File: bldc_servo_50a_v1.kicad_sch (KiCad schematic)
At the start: 130 parts, among them IC1 DRV8305NQPHPRQ1, IC2 TPS22919DCKR, J1 CAN1, J2 CAN2, J3 SWD, J4 SWD, J5 FAN, P1 PVDD, P2 GND, P3 PHASE_A, P4 PHASE_B, P5 PHASE_C, Q1 BSC010N04LS, Q2 BSC010N04LS, Q3 BSC010N04LS, Q4 BSC010N04LS, Q5 BSC010N04LS, Q6 BSC010N04LS, U1 TLV75533PDBV, U2 SN65HVD230, U3 LMR51430, U5 STM32G431CBT6

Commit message: Wip: before fixing footprints
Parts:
- added C54, C55, C56: 1n, Capacitor_SMD:C_0402_1005Metric_Pad0.74x0.62mm_HandSolder, symbol Device:C_Small
- L1: value 3.3uH -> 3.3u
- renumbered C45 to C1, C13 to C10, C14 to C11, C15 to C12, C27 to C13, C50 to C14, C17 to C15, C38 to C16, C40 to C17, C41 to C18, C51 to C19, C44 to C2, C52 to C20, C19 to C21, C20 to C22, C21 to C23, C22 to C24, C23 to C25, C30 to C26, C32 to C27, C29 to C28, C39 to C29, C46 to C3, C8 to C30, C5 to C31, C1 to C32, C7 to C33, C9 to C34, C3 to C35, C2 to C36, C6 to C37, C28 to C38, C34 to C39, C47 to C4, C36 to C40, C33 to C41, C35 to C42, C31 to C43, C12 to C44, C16 to C45, C18 to C46, C43 to C47, C42 to C48, C37 to C49, C48 to C5, C24 to C50, C25 to C51, C26 to C52, C49 to C6, C10 to C7, C4 to C8, C11 to C9, D2 to D1, D3 to D2, D6 to D3, D7 to D6, J5 to J3, J3 to J4, J4 to J5, NT5 to NT1, NT11 to NT10, NT3 to NT11, NT4 to NT2, NT6 to NT3, NT1 to NT4, NT7 to NT5, NT8 to NT6, NT2 to NT7, NT9 to NT8, NT10 to NT9, R5 to R1, R6 to R10, R28 to R11, R3 to R12, R4 to R13, R19 to R14, R20 to R15, R14 to R16, R29 to R17, R31 to R18, R33 to R19, R9 to R2, R35 to R20, R30 to R21, R32 to R22, R34 to R23, R36 to R24, R15 to R25, R16 to R26, R17 to R27, R23 to R28, R18 to R3, R1 to R4, R2 to R5, R7 to R6, R8 to R7, R12 to R8, R13 to R9, U5 to U1, IC1 to U2, U1 to U4, U2 to U5, IC2 to U6
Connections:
- net PWRGD is gone; now on net DRV_PWRGD: U1.25 (PB11)
- net WAKE is gone; now on net DRV_WAKE: U1.3 (PC14)
- net +3.3V: now also C21.2, C22.2, C23.2, C24.2, C25.2; no longer C21.1, C22.1, C23.1, C24.1, C25.1
- net +5V: now also L1.1; no longer L1.2
- net 5V_SW: now also L1.2; no longer L1.1
- net DRV_WAKE: no longer U1.40 (PB3)
- net FAN_EN: now also U1.44 (PB7)
- net GND: now also C21.1, C22.1, C23.1, C24.1, C25.1, C54.2, C55.2, C56.2; no longer C21.2, C22.2, C23.2, C24.2, C25.2
- net PHASE_A_SENSE: now also U1.10 (PA2); no longer U1.11 (PA3)
- net PHASE_B_SENSE: now also U1.11 (PA3); no longer U1.5 (PF0)
- net PVDD_SENSE: now also U1.5 (PF0); no longer U1.6 (PF1)
- net SO1: now also U1.6 (PF1); no longer U1.8 (PA0)
- net SO2: now also U1.8 (PA0); no longer U1.9 (PA1)
- net SO3: now also U1.9 (PA1); no longer U1.10 (PA2)
- net at NT1.2, NT2.2, Q2.1 (S_1)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: now also C54.1
- net BOOT0: now reaches U1.45 (PB8)
- net at NT5.2, NT6.2, Q4.1 (S_1)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: now also C55.1
- net at NT10.2, NT9.2, Q6.1 (S_1)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: now also C56.1
- net FAN renamed FAN_PWM
- net SCLK renamed SCK
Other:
- note added: "3.3V LDO"
- note added: "5V BUCK CONVERTER"
- note added: "CAN TRANSCEIVER"
- note added: "DRIVER"
- note added: "FAN CONTROL"
- note added: "LED"
- note added: "MAIN VOLTAGE CAPACITORS"
- note added: "MOSFETS"
- note added: "MOUNTING HOLES"
- note added: "TEMPERATURE SENSING"
- note added: "VOLTAGE SENSING"
- note added: "tentative"
- note removed: "5v regulator"
- note removed: "Addressable LED"
- note removed: "CAN Transceiver"
- note removed: "DRV8305"
- note removed: "Encoder Connectors"
- note removed: "LDO (5v->3v3)"
- note removed: "MCU Decoupling caps"
- note removed: "Mosfets"
- note removed: "Phase Voltage Sensing"
- note removed: "RC Snubber"
- note removed: "SWD"
- note removed: "Thermistor"
- moved on the sheet: C1, C10, C11, C12, C13, C14, C15, C16, C17, C18, C19, C2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

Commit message: Schematic done
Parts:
- FPC1, FPC2: footprint HCTL HC-FPC-05-09-8RLTAG_8pin connector:FPC-SMD_8P-P0.50_HC-FPC-05-09-8RLTAG -> HCTL HC-FPC-05-09-8RLTAG:FPC-SMD_8P-P0.50_HC-FPC-05-09-8RLTAG
- U6: footprint SOT65P210X110-6N -> TPS22919DCKR:SOT65P210X110-6N
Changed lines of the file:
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@@
 			)
 		)
-		(property "Footprint" "HCTL HC-FPC-05-09-8RLTAG_8pin connector:FPC-SMD_8P-P0.50_HC-FPC-05-09-8RLTAG"
+		(property "Footprint" "HCTL HC-FPC-05-09-8RLTAG:FPC-SMD_8P-P0.50_HC-FPC-05-09-8RLTAG"
 			(at 322.58 154.94 0)
 			(effects
@@
 			)
 		)
-		(property "Footprint" "HCTL HC-FPC-05-09-8RLTAG_8pin connector:FPC-SMD_8P-P0.50_HC-FPC-05-09-8RLTAG"
+		(property "Footprint" "HCTL HC-FPC-05-09-8RLTAG:FPC-SMD_8P-P0.50_HC-FPC-05-09-8RLTAG"
 			(at 322.58 115.57 0)
 			(effects
@@
 			)
 		)
-		(property "Footprint" "SOT65P210X110-6N"
+		(property "Footprint" "TPS22919DCKR:SOT65P210X110-6N"
 			(at 232.41 220.65 0)
 			(effects

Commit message: Some small changes
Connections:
- net NFAULT is gone; now on net DRV_NFAULT: U1.22 (PB10), U2.8 (NFAULT)
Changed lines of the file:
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@@
 	(wire
 		(pts
-			(xy 24.13 63.5) (xy 31.75 63.5)
+			(xy 21.59 63.5) (xy 31.75 63.5)
 		)
 		(stroke
@@
 	(wire
 		(pts
-			(xy 24.13 83.82) (xy 31.75 83.82)
+			(xy 21.59 83.82) (xy 31.75 83.82)
 		)
 		(stroke
@@
 	(wire
 		(pts
-			(xy 24.13 71.12) (xy 31.75 71.12)
+			(xy 21.59 71.12) (xy 31.75 71.12)
 		)
 		(stroke
@@
 	(wire
 		(pts
-			(xy 24.13 73.66) (xy 31.75 73.66)
+			(xy 21.59 73.66) (xy 31.75 73.66)
 		)
 		(stroke
@@
 	(wire
 		(pts
-			(xy 24.13 68.58) (xy 31.75 68.58)
+			(xy 21.59 68.58) (xy 31.75 68.58)
 		)
 		(stroke
@@
 	(wire
 		(pts
-			(xy 24.13 81.28) (xy 31.75 81.28)
-		)
-		(stroke
-			(width 0)
-			(type default)
-		)
-	)
-	(wire
-		(pts
 			(xy 335.28 100.33) (xy 351.79 100.33)
 		)
@@
 	(wire
 		(pts
-			(xy 24.13 86.36) (xy 31.75 86.36)
+			(xy 21.59 86.36) (xy 31.75 86.36)
 		)
 		(stroke
@@
 	(wire
 		(pts
-			(xy 24.13 88.9) (xy 31.75 88.9)
+			(xy 21.59 88.9) (xy 31.75 88.9)
 		)
 		(stroke
@@
 	(wire
 		(pts
-			(xy 24.13 78.74) (xy 31.75 78.74)
+			(xy 21.59 78.74) (xy 31.75 78.74)
 		)
 		(stroke
@@
 	(wire
 		(pts
-			(xy 24.13 76.2) (xy 31.75 76.2)
+			(xy 21.59 76.2) (xy 31.75 76.2)
 		)
 		(stroke
@@
 	(wire
 		(pts
-			(xy 24.13 91.44) (xy 31.75 91.44)
+			(xy 21.59 91.44) (xy 31.75 91.44)
 		)
 		(stroke
@@
 	(wire
 		(pts
+			(xy 21.59 81.28) (xy 31.75 81.28)
+		)
+		(stroke
+			(width 0)
+			(type default)
+		)
+	)
+	(wire
+		(pts
 			(xy 226.06 201.93) (xy 234.95 201.93)
 		)
@@
 	(wire
 		(pts
-			(xy 24.13 66.04) (xy 31.75 66.04)
+			(xy 21.59 66.04) (xy 31.75 66.04)
 		)
 		(stroke
@@
 	)
 	(label "INHA"
-		(at 24.13 66.04 0)
+		(at 21.59 66.04 0)
 		(effects
 			(font
@@
 	)
 	(label "MOSI"
-		(at 24.13 86.36 0)
+		(at 21.59 86.36 0)
 		(effects
 			(font
@@
 	)
 	(label "DRV_CS"
-		(at 24.13 83.82 0)
+		(at 21.59 83.82 0)
 		(effects
 			(font
@@
 		)
 	)
+	(label "DRV_NFAULT"
+		(at 335.28 87.63 0)
+		(effects
+			(font
+				(size 1.27 1.27)
+			)
+			(justify left bottom)
+		)
+	)
 	(label "SL_C"
 		(at 83.82 88.9 180)
@@
 	)
 	(label "INLC"
-		(at 24.13 78.74 0)
+		(at 21.59 78.74 0)
 		(effects
 			(font
@@
 		)
 	)
-	(label "NFAULT"
-		(at 24.13 81.28 0)
-		(effects
-			(font
-				(size 1.27 1.27)
-			)
-			(justify left bottom)
-		)
-	)
 	(label "DRV_AVDD"
 		(at 16.51 152.4 0)
@@
 	)
 	(label "INHB"
-		(at 24.13 71.12 0)
+		(at 21.59 71.12 0)
 		(effects
 			(font
@@
 	)
 	(label "INLA"
-		(at 24.13 68.58 0)
+		(at 21.59 68.58 0)
 		(effects
 			(font
@@
 		)
 	)
+	(label "DRV_NFAULT"
+		(at 21.59 81.28 0)
+		(effects
+			(font
+				(size 1.27 1.27)
+			)
+			(justify left bottom)
+		)
+	)
 	(label "FAN_PWM"
 		(at 218.44 102.87 180)
@@
 	)
 	(label "SCK"
-		(at 24.13 91.44 0)
+		(at 21.59 91.44 0)
 		(effects
 			(font
@@
 	)
 	(label "INHC"
-		(at 24.13 76.2 0)
+		(at 21.59 76.2 0)
 		(effects
 			(font
@@
 	)
 	(label "MISO"
-		(at 24.13 88.9 0)
+		(at 21.59 88.9 0)
 		(effects
 			(font
@@
 	)
 	(label "EN_GATE"
-		(at 24.13 63.5 0)
+		(at 21.59 63.5 0)
 		(effects
 			(font
@@
 		)
 	)
-	(label "NFAULT"
-		(at 335.28 87.63 0)
-		(effects
-			(font
-				(size 1.27 1.27)
-			)
-			(justify left bottom)
-		)
-	)
 	(label "SH_C"
 		(at 138.4256 223.52 0)
@@
 	)
 	(label "INLB"
-		(at 24.13 73.66 0)
+		(at 21.59 73.66 0)
 		(effects
 			(font
@@
 	(symbol
 		(lib_id "power:PWR_FLAG")
-		(at 383.54 267.97 270)
+		(at 393.7 266.7 270)
 		(unit 1)
 		(exclude_from_sim no)
@@
 		(dnp no)
 		(property "Reference" "#FLG04"
-			(at 385.445 267.97 0)
+			(at 395.605 266.7 0)
 			(effects
 				(font
@@
 		)
 		(property "Value" "PWR_FLAG"
-			(at 387.096 267.97 0)
+			(at 397.256 266.7 0)
 			(effects
 				(font
@@
 		)
 		(property "Footprint" ""
-			(at 383.54 267.97 0)
+			(at 393.7 266.7 0)
 			(effects
 				(font
@@
 		)
 		(property "Datasheet" "~"
-			(at 383.54 267.97 0)
+			(at 393.7 266.7 0)
 			(effects
 				(font
@@
 		)
 		(property "Description" "Special symbol for telling ERC where power comes from"
-			(at 383.54 267.97 0)
+			(at 393.7 266.7 0)
 			(effects
 				(font
@@
 	(symbol
 		(lib_id "power:+3V3")
-		(at 383.54 267.97 0)
+		(at 393.7 266.7 0)
 		(unit 1)
 		(exclude_from_sim no)
@@
 		(dnp no)
 		(property "Reference" "#PWR055"
-			(at 383.54 271.78 0)
+			(at 393.7 270.51 0)
 			(effects
 				(font
@@
 		)
 		(property "Value" "+3V3"
-			(at 383.54 264.414 0)
+			(at 393.7 263.144 0)
 			(effects
 				(font
@@
 		)
 		(property "Footprint" ""
-			(at 383.54 267.97 0)
+			(at 393.7 266.7 0)
 			(effects
 				(font
@@
 		)
 		(property "Datasheet" ""
-			(at 383.54 267.97 0)
+			(at 393.7 266.7 0)
 			(effects
 				(font
@@
 		)
 		(property "Description" "Power symbol creates a global label with name \"+3V3\""
-			(at 383.54 267.97 0)
+			(at 393.7 266.7 0)
 			(effects
 				(font

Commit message: Tentative placement of FETs in PCB
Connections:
- net SN1: now also NT4.1; no longer NT2.1
- net SN2: now also NT7.1; no longer NT6.1
- net SN3: now also NT11.1; no longer NT10.1
- net SP1: now also NT2.1; no longer NT4.1
- net SP2: now also NT6.1; no longer NT7.1
- net SP3: now also NT10.1; no longer NT11.1

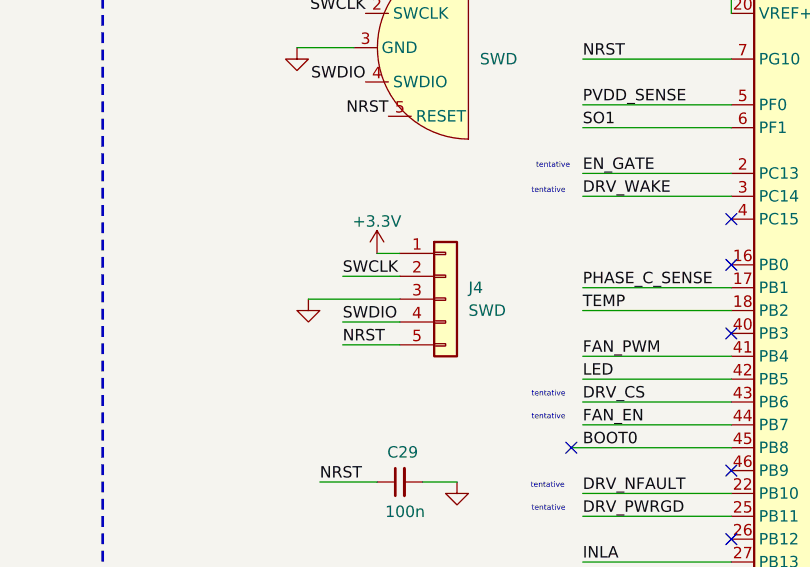
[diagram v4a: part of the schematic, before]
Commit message: Placing DRV, Bulk caps, FETs
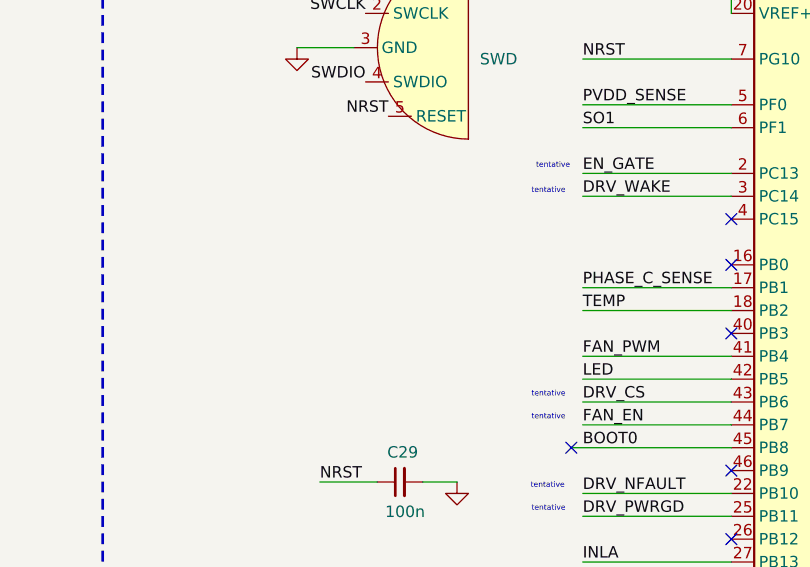
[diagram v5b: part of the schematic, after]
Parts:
- removed J4: SWD, Connector_PinHeader_2.54mm:PinHeader_1x05_P2.54mm_Vertical, symbol Connector_Generic:Conn_01x05

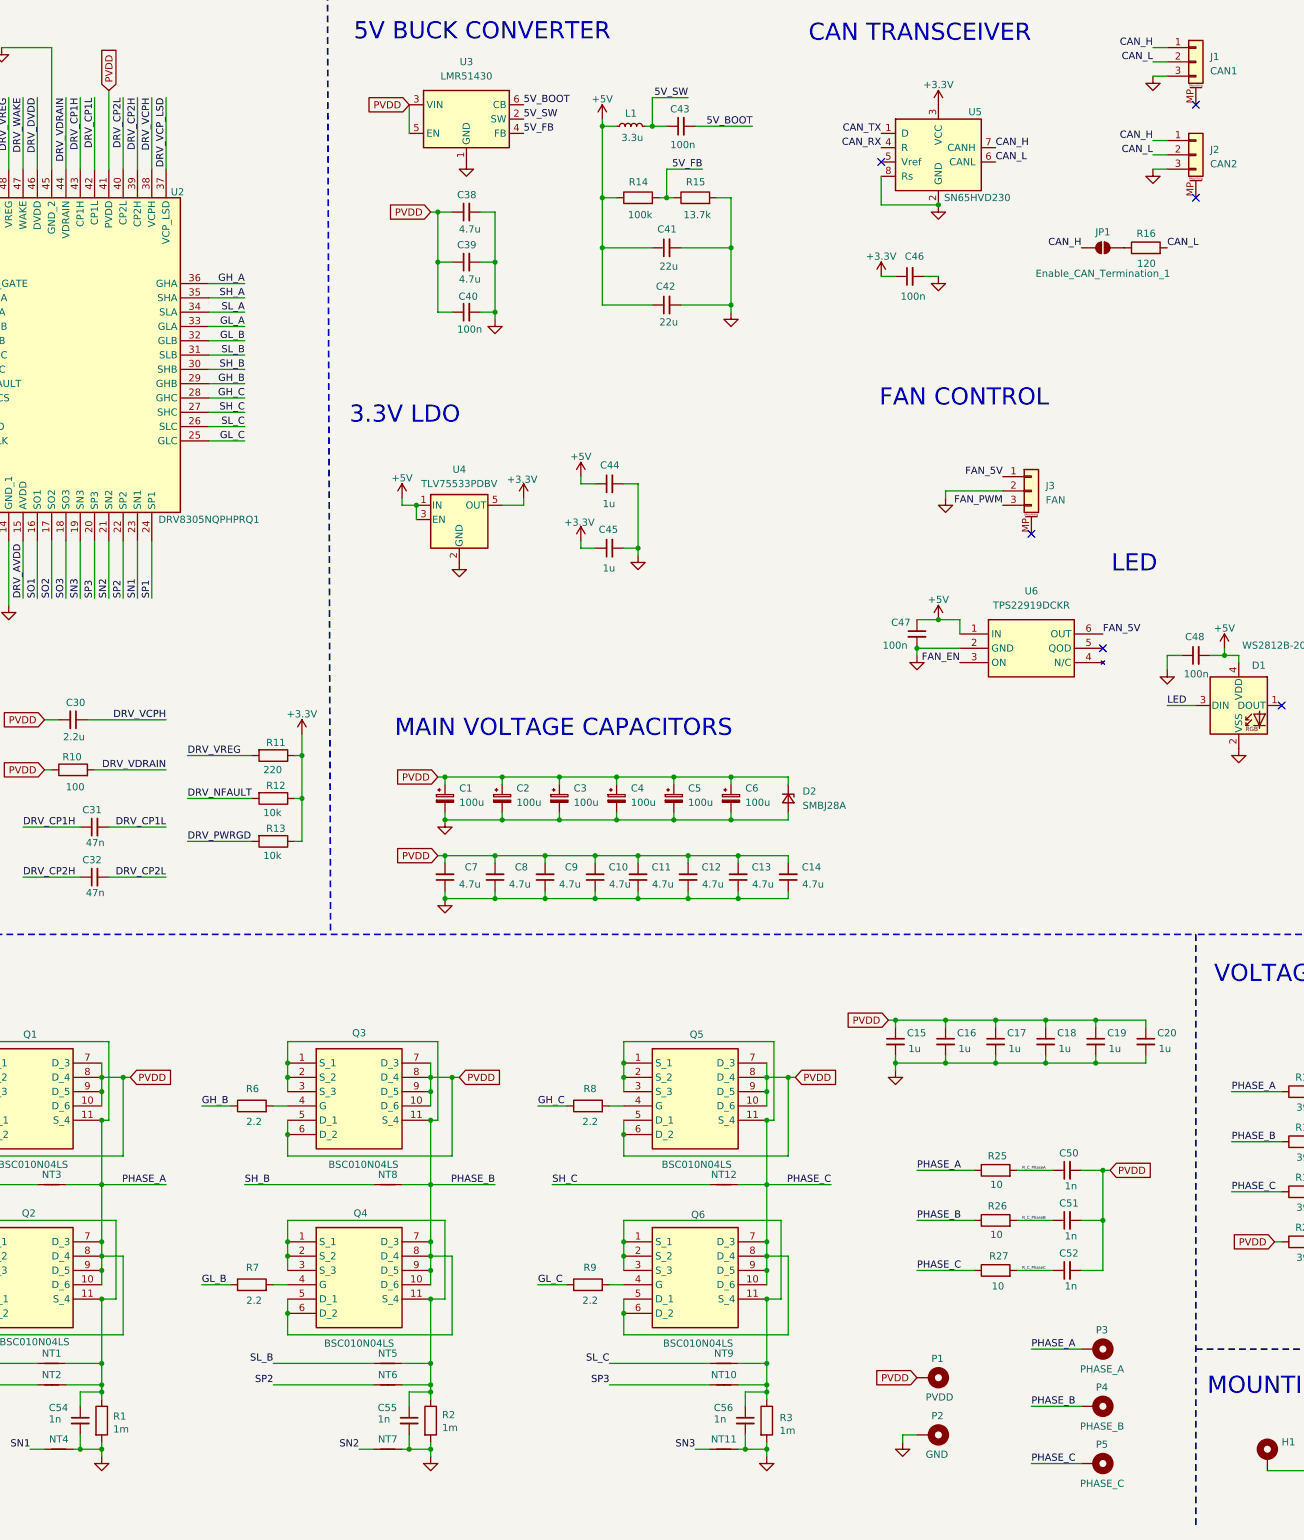
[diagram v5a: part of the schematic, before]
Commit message: Placement changed
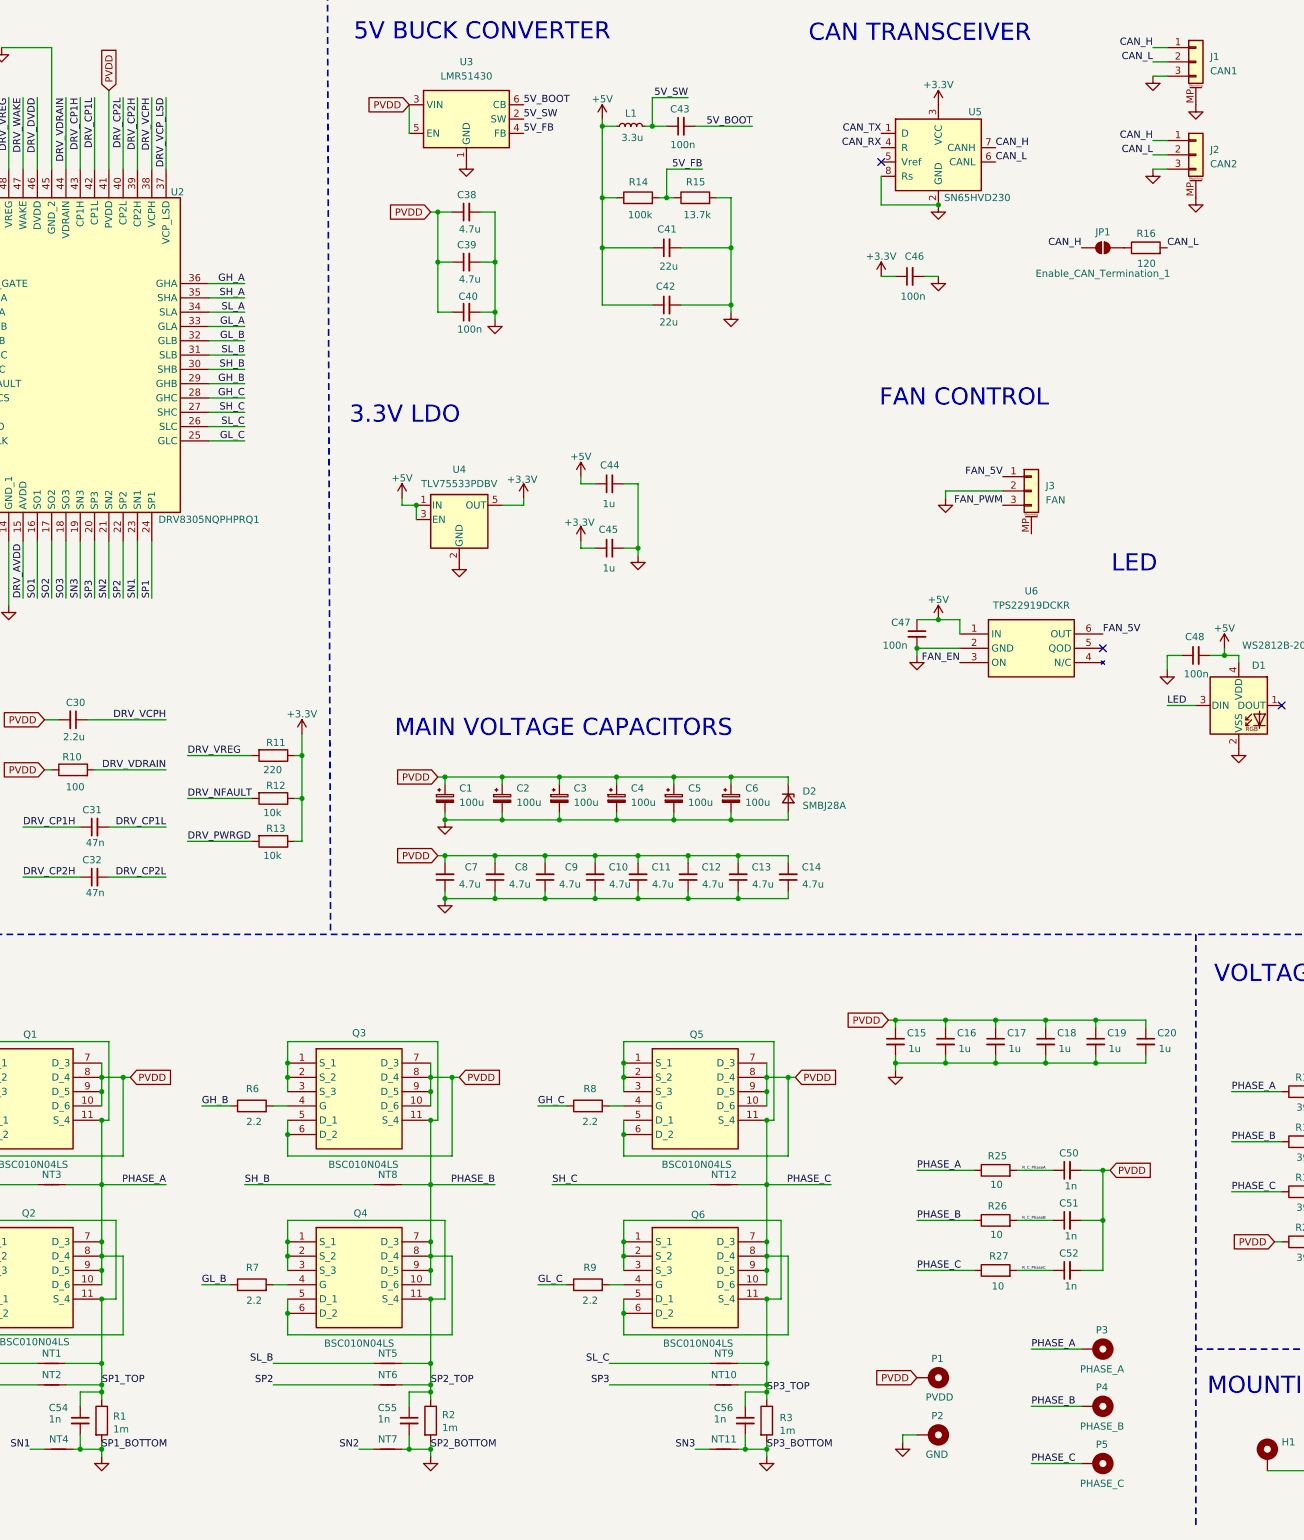
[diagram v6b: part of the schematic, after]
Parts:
- H1, H2, H3: value ~ -> (none)
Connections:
- net GND: now also J1.MP (MountPin), J2.MP (MountPin)
- net SP1_TOP: now reaches C54.1, NT1.2, NT2.2, Q2.1 (S_1), Q2.11 (S_4), Q2.2 (S_2), Q2.3 (S_3), R1.1
- net SP3_TOP: now reaches C56.1, NT10.2, NT9.2, Q6.1 (S_1), Q6.11 (S_4), Q6.2 (S_2), Q6.3 (S_3), R3.1
- net SP2_TOP: now reaches C55.1, NT5.2, NT6.2, Q4.1 (S_1), Q4.11 (S_4), Q4.2 (S_2), Q4.3 (S_3), R2.1
- no-connect marks 16 -> 13

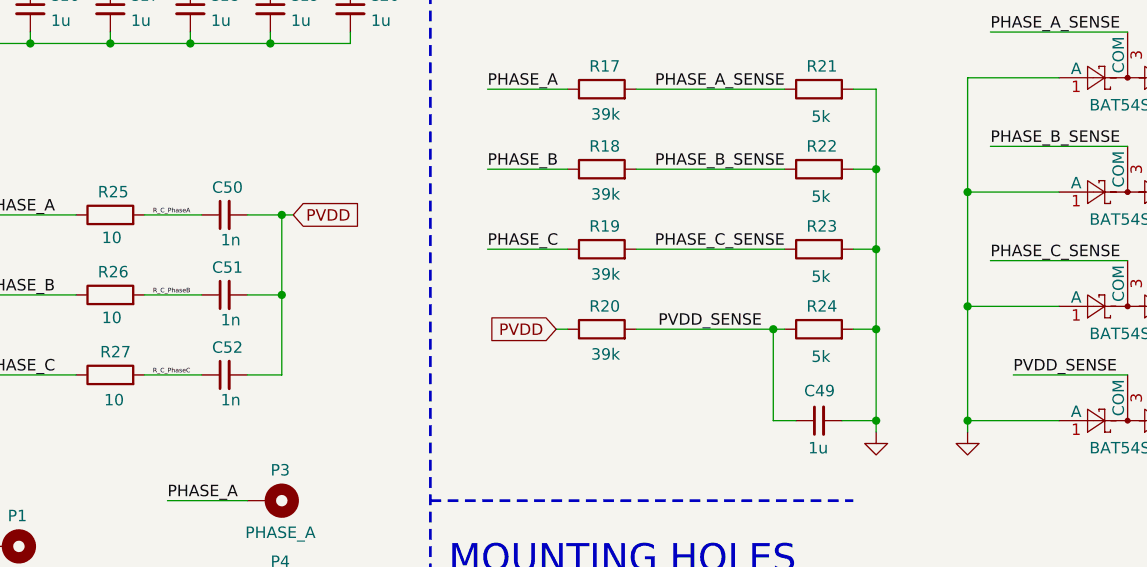
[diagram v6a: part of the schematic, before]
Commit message: Changed Phases placement
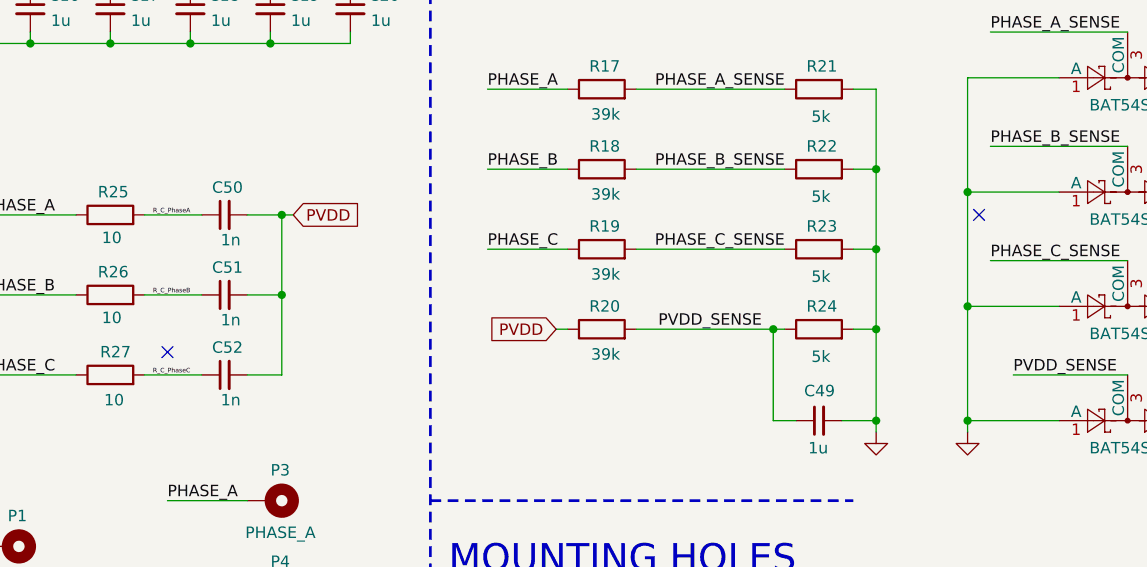
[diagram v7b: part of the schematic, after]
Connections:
- no-connect marks 13 -> 15
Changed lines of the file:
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@@
+	)
+	(no_connect
+		(at 223.52 236.22)
 	)
 	(no_connect
@@
 	)
 	(no_connect
+		(at 313.69 220.98)
+	)
+	(no_connect
